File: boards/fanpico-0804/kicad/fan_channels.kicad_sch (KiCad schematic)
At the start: 12 parts, among them J10 Fan3 Output, J11 Fan4 Output, J12 Fan5 Output, J13 Fan6 Output, J14 Fan7 Output, J15 Fan8 Output, J4 Fan1 Input, J5 Fan2 Input, J6 Fan3 Input, J7 Fan4 Input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

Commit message: PCB version 1.2
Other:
- title: FanPico-0804 -> FanPico-0804 v1.2
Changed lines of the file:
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@@
   (paper "A4")
   (title_block
-    (title "FanPico-0804")
-    (date "2022-02-26")
+    (title "FanPico-0804 v1.2")
+    (date "2022-03-11")
     (company "Timo Kokkonen <tjko@iki.fi>")
-    (comment 3 "Fanpico firmware reference/prototype PCB.")
+    (comment 3 "Fanpico firmware reference PCB.")
   )
   (junction (at 57.15 93.98) (diameter 0) (color 0 0 0 0)

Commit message: New PCB revision v1.3
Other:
- title: FanPico-0804 v1.2 -> FanPico-0804 v1.3
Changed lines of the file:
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@@
   (paper "A4")
   (title_block
-    (title "FanPico-0804 v1.2")
-    (date "2022-03-11")
+    (title "FanPico-0804 v1.3")
+    (date "2022-04-10")
     (company "Timo Kokkonen <tjko@iki.fi>")
     (comment 3 "Fanpico firmware reference PCB.")

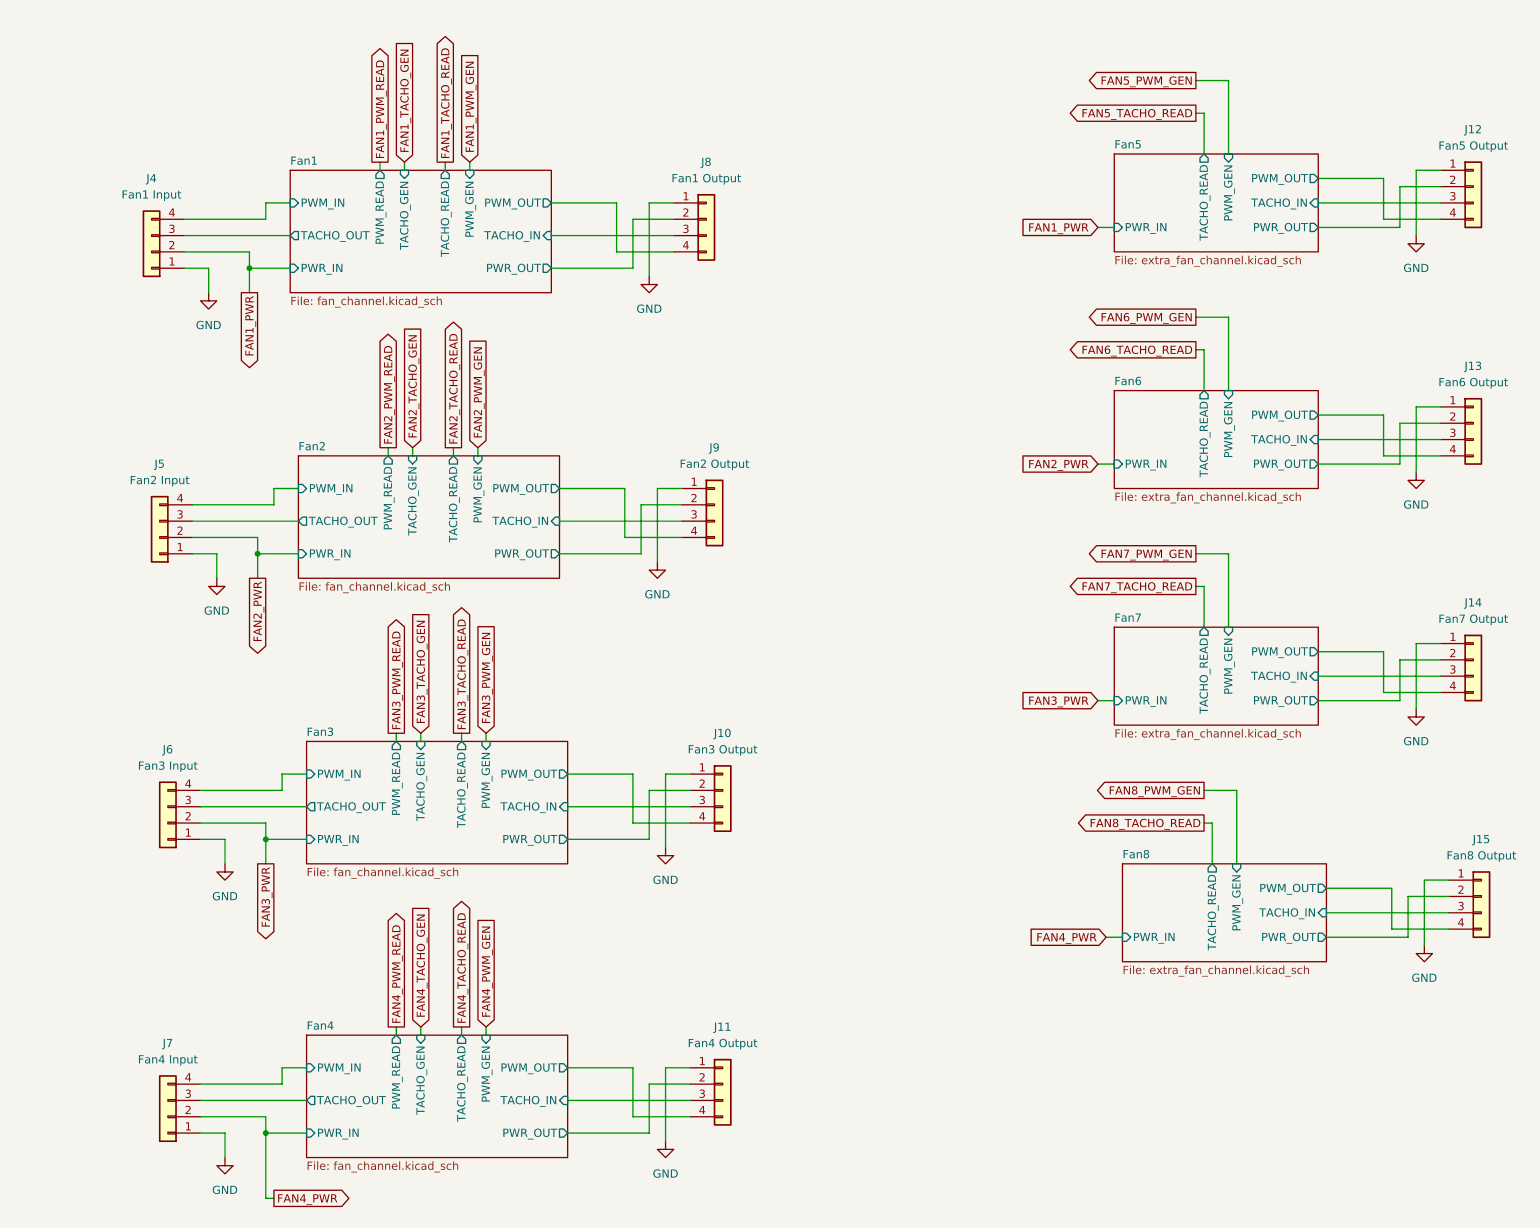
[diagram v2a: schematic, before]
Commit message: Cleanup schematic (no actual changes that affect PCB).
- Add labels to sub-pages so printed schematic is more readable.
- Rename FANx_PWM_READ to MBFANx_PWM_READ
- Rename FANx_TACHO_GEN to MBFANx_TACHO_GEN
- Use standard (KiCAD) footprints for the ICs (U1-U3)
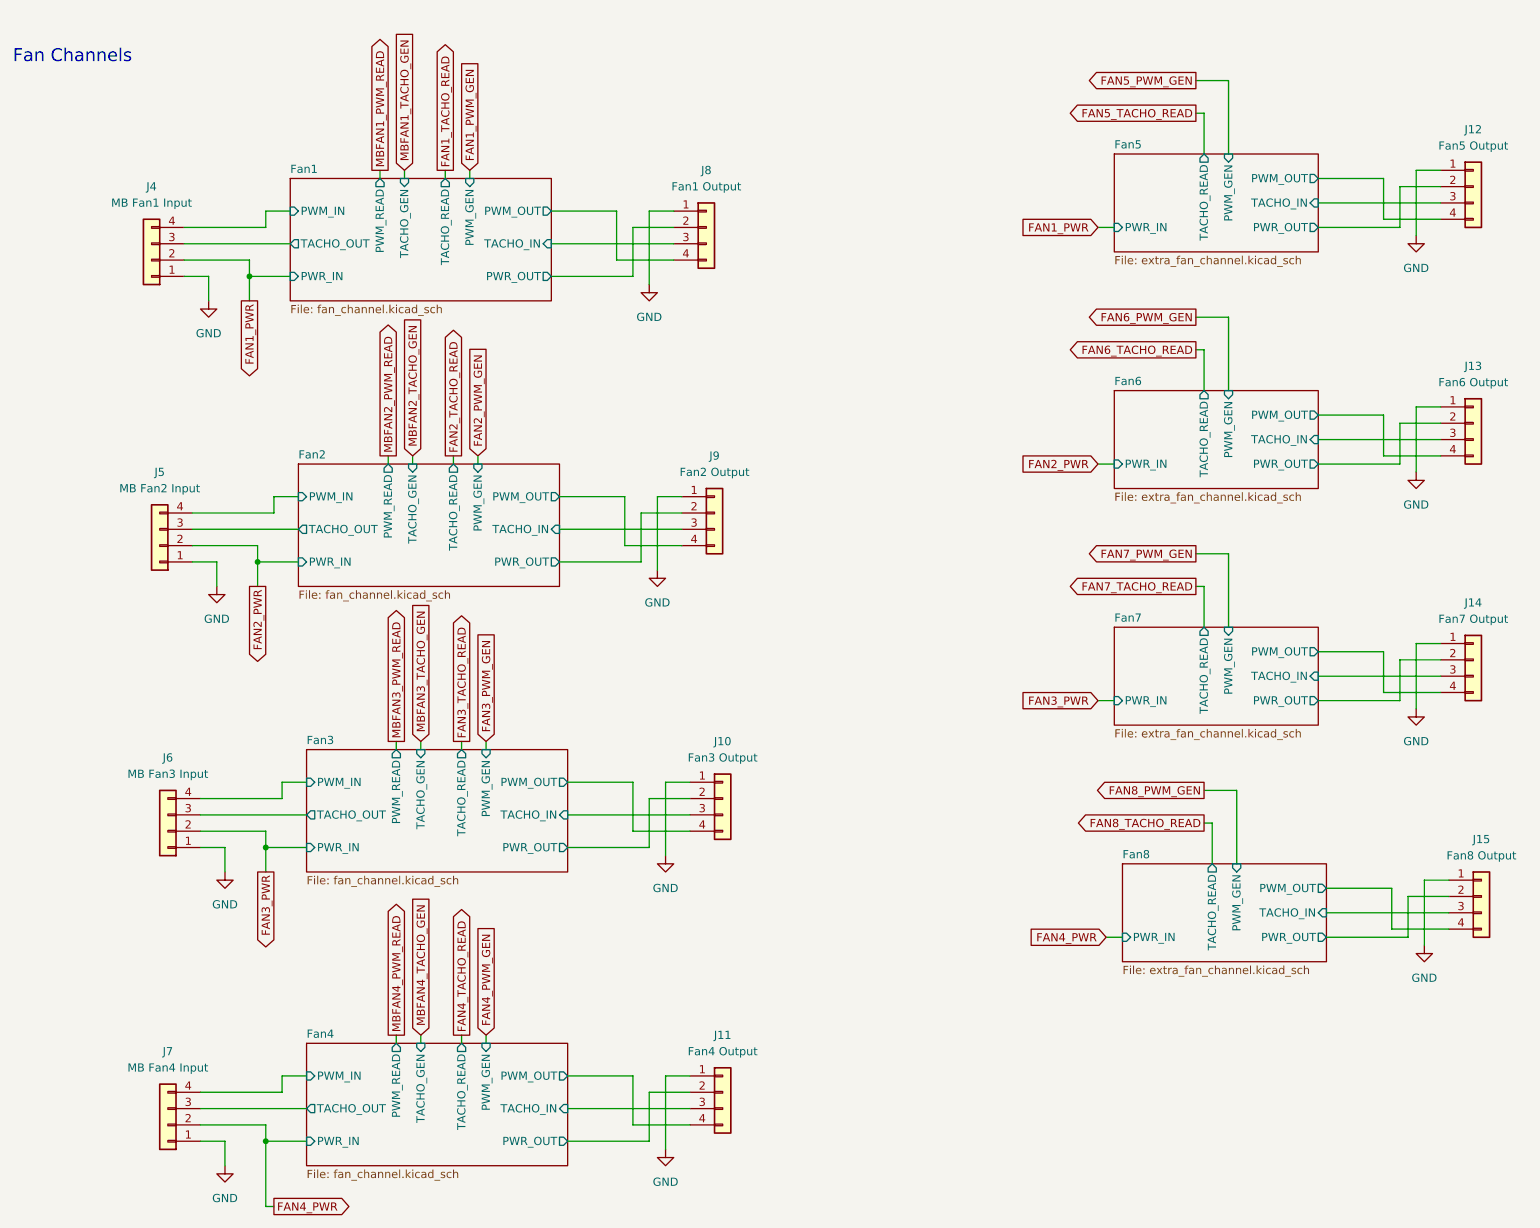
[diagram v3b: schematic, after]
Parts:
- J4: value Fan1 Input -> MB Fan1 Input
- J5: value Fan2 Input -> MB Fan2 Input
- J6: value Fan3 Input -> MB Fan3 Input
- J7: value Fan4 Input -> MB Fan4 Input
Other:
- note added: "Fan Channels"
- moved on the sheet: J10, J11, J4, J5, J6, J7, J8, J9
